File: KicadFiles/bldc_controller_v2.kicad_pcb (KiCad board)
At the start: 2 copper layers, 50 x 99 mm, 184 parts, among them J1 Conn_01x06_Male, J10 Conn_01x02_Female, J11 Conn_01x02_Female, J12 Conn_01x02_Female, J13 Conn_01x02_Female, J14 Conn_01x02_Female, J15 Conn_01x04_Male, J2 Conn_01x03_Male, J3 Conn_01x03_Male, J4 Screw_Terminal, J5 Conn_01x02_Female, J9 Conn_01x02_Female, Q1 DMN65D8L-7, Q10 IRLB8721PBF, Q11 IRLB8721PBF, Q2 DMN65D8L-7, Q3 DMN65D8L-7, Q4 DMN65D8L-7, Q5 IRF4905, Q6 IRLB8721PBF, Q7 IRLB8721PBF, Q8 IRLB8721PBF, Q9 IRLB8721PBF, SW2 D6C40 F1 LFS, SW3 1301.9314, SW4 1301.9314, SW5 SW_Push_DPDT, U1 ATmega328P-PU, U2 uA7810, U3 LM7805_TO220, U4 MCP601-xP, U5 LM339, U6 IRS2004, U7 IRS2004, U8 IRS2004, U9 HCPL-181-00DE, Y1 9B-16.000MBBK-B

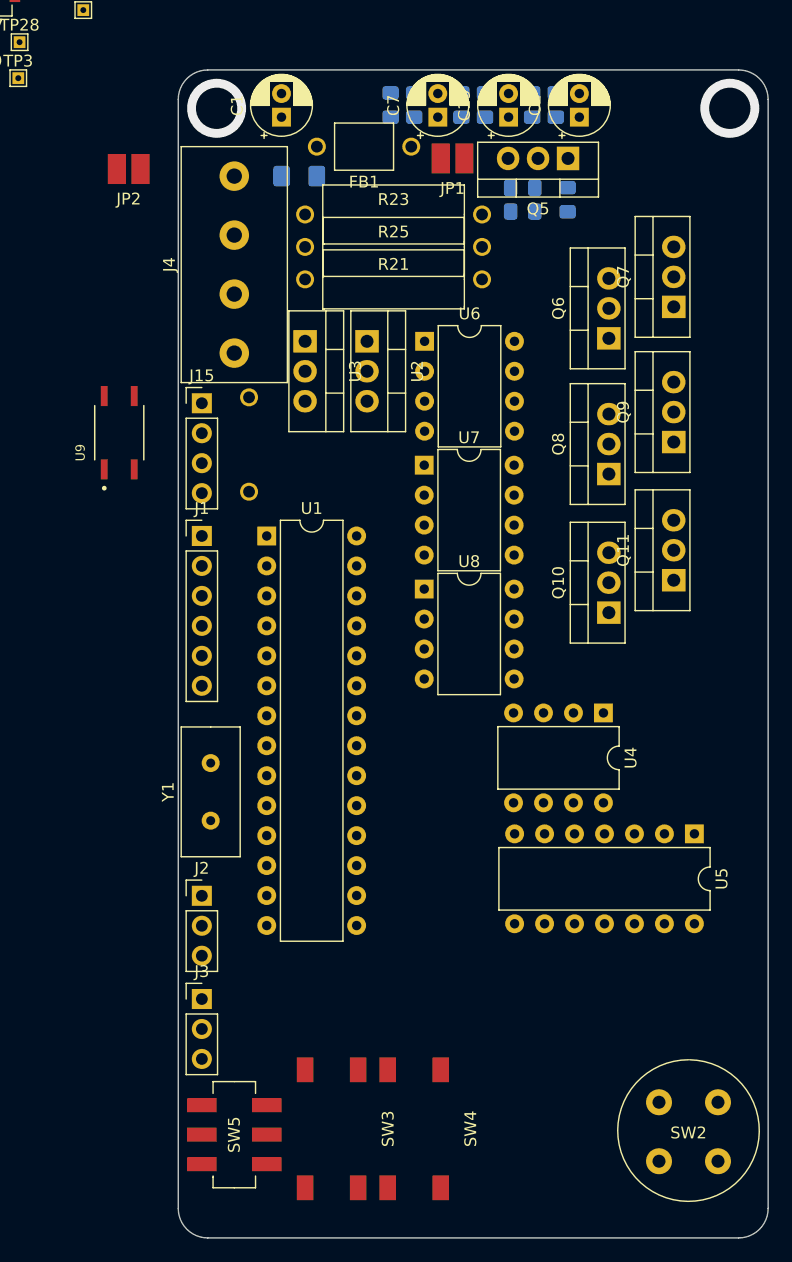
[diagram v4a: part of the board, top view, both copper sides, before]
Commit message: Updated Major Parts Placement
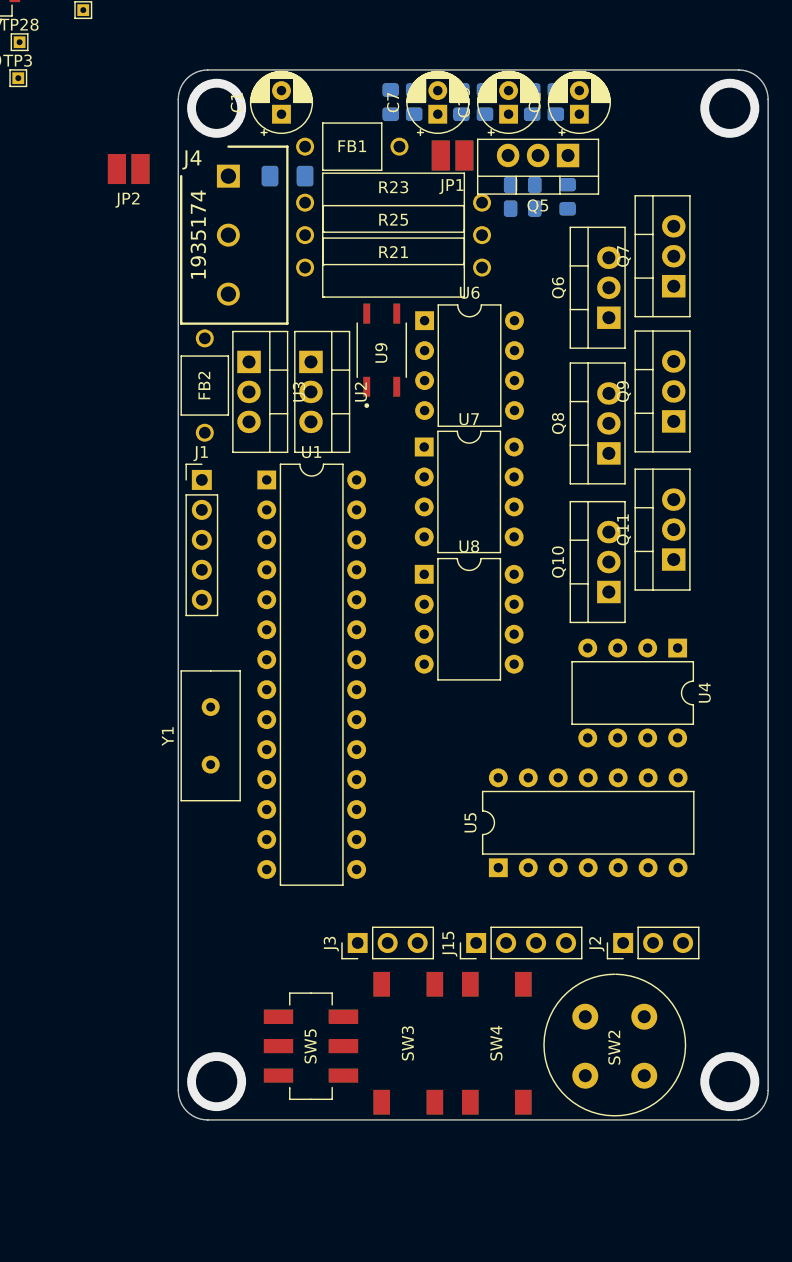
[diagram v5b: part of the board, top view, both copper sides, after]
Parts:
- FB2: moved to F.Cu
- J1: value Conn_01x06_Male -> Conn_01x05_Male; footprint Connector_PinHeader_2.54mm:PinHeader_1x06_P2.54mm_Vertical -> Connector_PinHeader_2.54mm:PinHeader_1x05_P2.54mm_Vertical
- J4: value Screw_Terminal -> 1935174; footprint Connector:Terminal_Block_4Pin_TH -> 1935174:SHDR3W110P0X500_1X3_1500X900X1140P
- moved J15 51.3 mm to (138.2, 135.0), turned to 90 degrees
- moved J2 35.9 mm to (150.7, 135.0), turned to 90 degrees
- moved U9 23.3 mm to (130.2, 84.8)
- moved U5 16.9 mm to (140.1, 128.6), turned to 90 degrees
- moved J3 14.0 mm to (128.2, 135.0), turned to 90 degrees
- moved SW4 10.1 mm to (142.2, 143.5)
- moved SW5 9.92 mm to (124.2, 143.8)
- moved SW3 9.74 mm to (134.8, 143.5)
- moved SW2 9.57 mm to (150.0, 146.2)
- moved U4 8.36 mm to (155.3, 110.0)
- moved J4 7.52 mm to (117.2, 70.0)
- moved FB2 6.25 mm to (115.2, 87.8)
- moved U2 5.06 mm to (124.2, 85.8)
- moved U3 5.06 mm to (119.0, 85.8)
- moved J1 4.75 mm to (115.0, 95.8)
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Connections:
- J1 pad 4: GNDD -> /TXD
- J1 pad 5: /TXD -> /RXD
- U5 pad 10: /NEUTRAL -> /I_SENSE
- U5 pad 11: /C_FILT -> /I_THRESH
- U5 pad 13: /BEMF_C -> Net-(R52-Pad1)
- U5 pad 2: Net-(R52-Pad1) -> /BEMF_C
- U5 pad 4: /I_SENSE -> /NEUTRAL
- U5 pad 5: /I_THRESH -> /C_FILT
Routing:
- net (no net): vias 2 -> 4
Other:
- board size 50 x 99 mm -> 50 x 89 mm

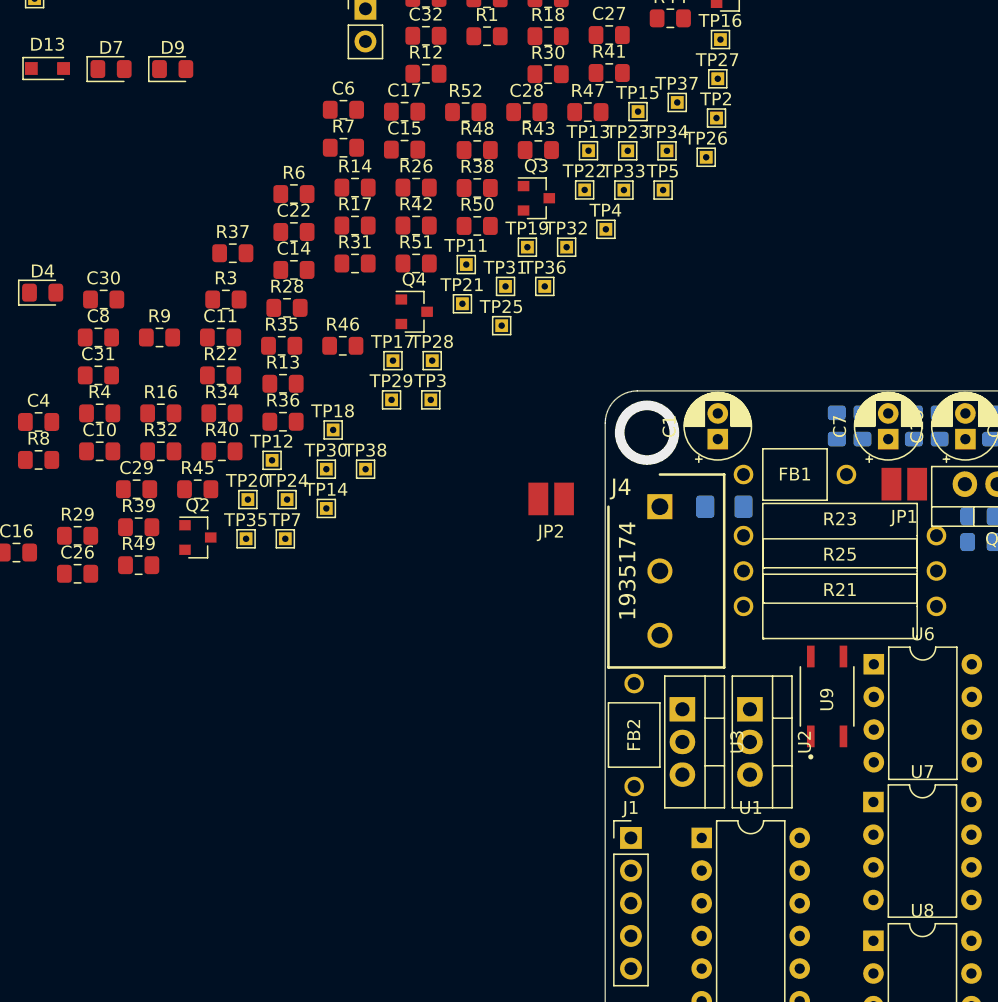
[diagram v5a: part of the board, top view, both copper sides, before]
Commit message: Replaced FB with Jumper
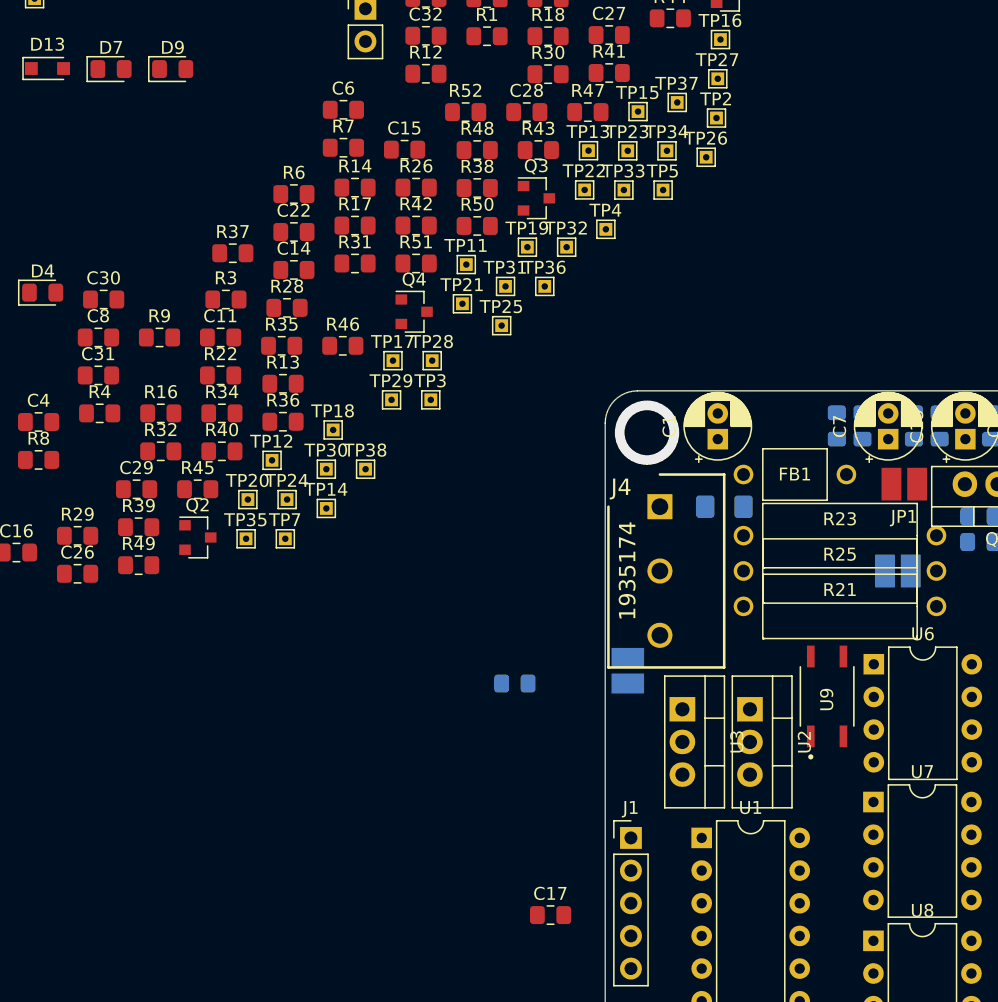
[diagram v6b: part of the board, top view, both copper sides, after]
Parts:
- removed FB2: BL01RN1A1D2B, Ferrite_THT:Ferrite_Bead_TH
- added JP3: SolderJumper_2_Open, Jumper:Solder_Jumper_2_Pin_5A, B.Cu at (114.8, 82.8)
- C10, JP2: moved to B.Cu
- moved C17 63.5 mm to (108.8, 101.8)
- moved C10 37.0 mm to (106.0, 83.8)
- moved JP2 27.5 mm to (135.8, 75.0)
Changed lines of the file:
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@@
     (add_net VBUS)
   )
+  (module Jumper:Solder_Jumper_2_Pin_5A (layer B.Cu)
+    (at 114.75 82.75 90)
+    (fp_text reference JP3 (at 0 -2.54 270) (layer B.SilkS)
+      (effects (font (size 1 1) (thickness 0.15)) (justify mirror))
+    )
+    (fp_text value SolderJumper_2_Open (at 0 -1.27 270) (layer B.Fab)
+      (effects (font (size 1 1) (thickness 0.15)) (justify mirror))
+    )
+    (pad 1 smd rect (at -1 0 90) (size 1.54 2.54) (layers B.Cu B.Paste B.Mask)
+      (net 4 GNDD))
+    (pad 2 smd rect (at 1 0 90) (size 1.54 2.54) (layers B.Cu B.Paste B.Mask)
+      (net 1 GNDPWR))
+  )
   (module Connector_PinHeader_2.54mm:PinHeader_1x05_P2.54mm_Vertical (layer F.Cu)
     (at 115 95.75)
@@
   )
   (module Ferrite_THT:Ferrite_Bead_TH (layer F.Cu)
-    (at 115.25 87.75 270)
-    (fp_text reference FB2 (at 0 0 90) (layer F.SilkS)
-      (effects (font (size 1 1) (thickness 0.15)))
-    )
-    (fp_text value BL01RN1A1D2B (at 0 3.1 90) (layer F.Fab)
-      (effects (font (size 1 1) (thickness 0.15)))
-    )
-    (fp_line (start 2.5 -2) (end -2.5 -2) (layer F.SilkS) (width 0.12))
-    (fp_line (start 2.5 2) (end 2.5 -2) (layer F.SilkS) (width 0.12))
-    (fp_line (start -2.5 2) (end 2.5 2) (layer F.SilkS) (width 0.12))
-    (fp_line (start -2.5 -2) (end -2.5 2) (layer F.SilkS) (width 0.12))
-    (pad 1 thru_hole circle (at -4 0 270) (size 1.524 1.524) (drill 1) (layers *.Cu *.Mask)
-      (net 1 GNDPWR))
-    (pad 2 thru_hole circle (at 4 0 270) (size 1.524 1.524) (drill 1) (layers *.Cu *.Mask)
-      (net 4 GNDD))
-  )
-  (module Ferrite_THT:Ferrite_Bead_TH (layer F.Cu)
     (at 127.75 67.5 180)
     (fp_text reference FB1 (at 0 0) (layer F.SilkS)
@@
     )
   )
-  (module Jumper:Solder_Jumper_2_Pin_5A (layer F.Cu)
-    (at 108.8 69.4)
-    (fp_text reference JP2 (at 0 2.54) (layer F.SilkS)
-      (effects (font (size 1 1) (thickness 0.15)))
+  (module Jumper:Solder_Jumper_2_Pin_5A (layer B.Cu)
+    (at 135.75 75)
+    (fp_text reference JP2 (at 0 -2.54) (layer B.SilkS)
+      (effects (font (size 1 1) (thickness 0.15)) (justify mirror))
     )
-    (fp_text value SolderJumper_2_Open (at 0 1.27) (layer F.Fab)
-      (effects (font (size 1 1) (thickness 0.15)))
+    (fp_text value SolderJumper_2_Open (at 0 -1.27) (layer B.Fab)
+      (effects (font (size 1 1) (thickness 0.15)) (justify mirror))
     )
-    (pad 1 smd rect (at -1 0) (size 1.54 2.54) (layers F.Cu F.Paste F.Mask)
+    (pad 1 smd rect (at -1 0) (size 1.54 2.54) (layers B.Cu B.Paste B.Mask)
       (net 1 GNDPWR))
-    (pad 2 smd rect (at 1 0) (size 1.54 2.54) (layers F.Cu F.Paste F.Mask)
+    (pad 2 smd rect (at 1 0) (size 1.54 2.54) (layers B.Cu B.Paste B.Mask)
       (net 47 /I_RAW))
   )
@@
   )
   (module Capacitor_SMD:C_0805_2012Metric_Pad1.15x1.40mm_HandSolder (layer F.Cu)
-    (at 97.400225 39.296)
+    (at 108.75 101.75)
     (descr "Capacitor SMD 0805 (2012 Metric), square (rectangular) end terminal, IPC_7351 nominal with elongated pad for handsoldering. (Body size source: https://docs.google.com/spreadsheets/d/1BsfQQcO9C6DZCsRaXUlFlo91Tg2WpOkGARC1WS5S8t0/edit?usp=sharing), generated with kicad-footprint-generator")
     (tags "capacitor handsolder")
@@
     )
   )
-  (module Capacitor_SMD:C_0805_2012Metric_Pad1.15x1.40mm_HandSolder (layer F.Cu)
-    (at 73.700225 65.696)
+  (module Capacitor_SMD:C_0805_2012Metric_Pad1.15x1.40mm_HandSolder (layer B.Cu)
+    (at 105.975 83.75)
     (descr "Capacitor SMD 0805 (2012 Metric), square (rectangular) end terminal, IPC_7351 nominal with elongated pad for handsoldering. (Body size source: https://docs.google.com/spreadsheets/d/1BsfQQcO9C6DZCsRaXUlFlo91Tg2WpOkGARC1WS5S8t0/edit?usp=sharing), generated with kicad-footprint-generator")
     (tags "capacitor handsolder")
     (attr smd)
-    (fp_text reference C10 (at 0 -1.65) (layer F.SilkS)
-      (effects (font (size 1 1) (thickness 0.15)))
+    (fp_text reference C10 (at 0 1.65) (layer B.SilkS)
+      (effects (font (size 1 1) (thickness 0.15)) (justify mirror))
     )
-    (fp_text value 1uF (at 0 1.65) (layer F.Fab)
-      (effects (font (size 1 1) (thickness 0.15)))
+    (fp_text value 1uF (at 0 -1.65) (layer B.Fab)
+      (effects (font (size 1 1) (thickness 0.15)) (justify mirror))
     )
-    (fp_text user %R (at 0 0) (layer F.Fab)
-      (effects (font (size 0.5 0.5) (thickness 0.08)))
+    (fp_line (start -1 -0.6) (end -1 0.6) (layer B.Fab) (width 0.1))
+    (fp_line (start -1 0.6) (end 1 0.6) (layer B.Fab) (width 0.1))
+    (fp_line (start 1 0.6) (end 1 -0.6) (layer B.Fab) (width 0.1))
+    (fp_line (start 1 -0.6) (end -1 -0.6) (layer B.Fab) (width 0.1))
+    (fp_line (start -0.261252 0.71) (end 0.261252 0.71) (layer B.SilkS) (width 0.12))
+    (fp_line (start -0.261252 -0.71) (end 0.261252 -0.71) (layer B.SilkS) (width 0.12))
+    (fp_line (start -1.85 -0.95) (end -1.85 0.95) (layer B.CrtYd) (width 0.05))
+    (fp_line (start -1.85 0.95) (end 1.85 0.95) (layer B.CrtYd) (width 0.05))
+    (fp_line (start 1.85 0.95) (end 1.85 -0.95) (layer B.CrtYd) (width 0.05))
+    (fp_line (start 1.85 -0.95) (end -1.85 -0.95) (layer B.CrtYd) (width 0.05))
+    (fp_text user %R (at 0 0) (layer B.Fab)
+      (effects (font (size 0.5 0.5) (thickness 0.08)) (justify mirror))
     )
-    (fp_line (start 1.85 0.95) (end -1.85 0.95) (layer F.CrtYd) (width 0.05))
-    (fp_line (start 1.85 -0.95) (end 1.85 0.95) (layer F.CrtYd) (width 0.05))
-    (fp_line (start -1.85 -0.95) (end 1.85 -0.95) (layer F.CrtYd) (width 0.05))
-    (fp_line (start -1.85 0.95) (end -1.85 -0.95) (layer F.CrtYd) (width 0.05))
-    (fp_line (start -0.261252 0.71) (end 0.261252 0.71) (layer F.SilkS) (width 0.12))
-    (fp_line (start -0.261252 -0.71) (end 0.261252 -0.71) (layer F.SilkS) (width 0.12))
-    (fp_line (start 1 0.6) (end -1 0.6) (layer F.Fab) (width 0.1))
-    (fp_line (start 1 -0.6) (end 1 0.6) (layer F.Fab) (width 0.1))
-    (fp_line (start -1 -0.6) (end 1 -0.6) (layer F.Fab) (width 0.1))
-    (fp_line (start -1 0.6) (end -1 -0.6) (layer F.Fab) (width 0.1))
-    (pad 2 smd roundrect (at 1.025 0) (size 1.15 1.4) (layers F.Cu F.Paste F.Mask) (roundrect_rratio 0.217391)
-      (net 4 GNDD))
-    (pad 1 smd roundrect (at -1.025 0) (size 1.15 1.4) (layers F.Cu F.Paste F.Mask) (roundrect_rratio 0.217391)
+    (pad 1 smd roundrect (at -1.025 0) (size 1.15 1.4) (layers B.Cu B.Paste B.Mask) (roundrect_rratio 0.217391)
       (net 7 +12V))
+    (pad 2 smd roundrect (at 1.025 0) (size 1.15 1.4) (layers B.Cu B.Paste B.Mask) (roundrect_rratio 0.217391)
+      (net 4 GNDD))
     (model ${KISYS3DMOD}/Capacitor_SMD.3dshapes/C_0805_2012Metric.wrl
       (at (xyz 0 0 0))

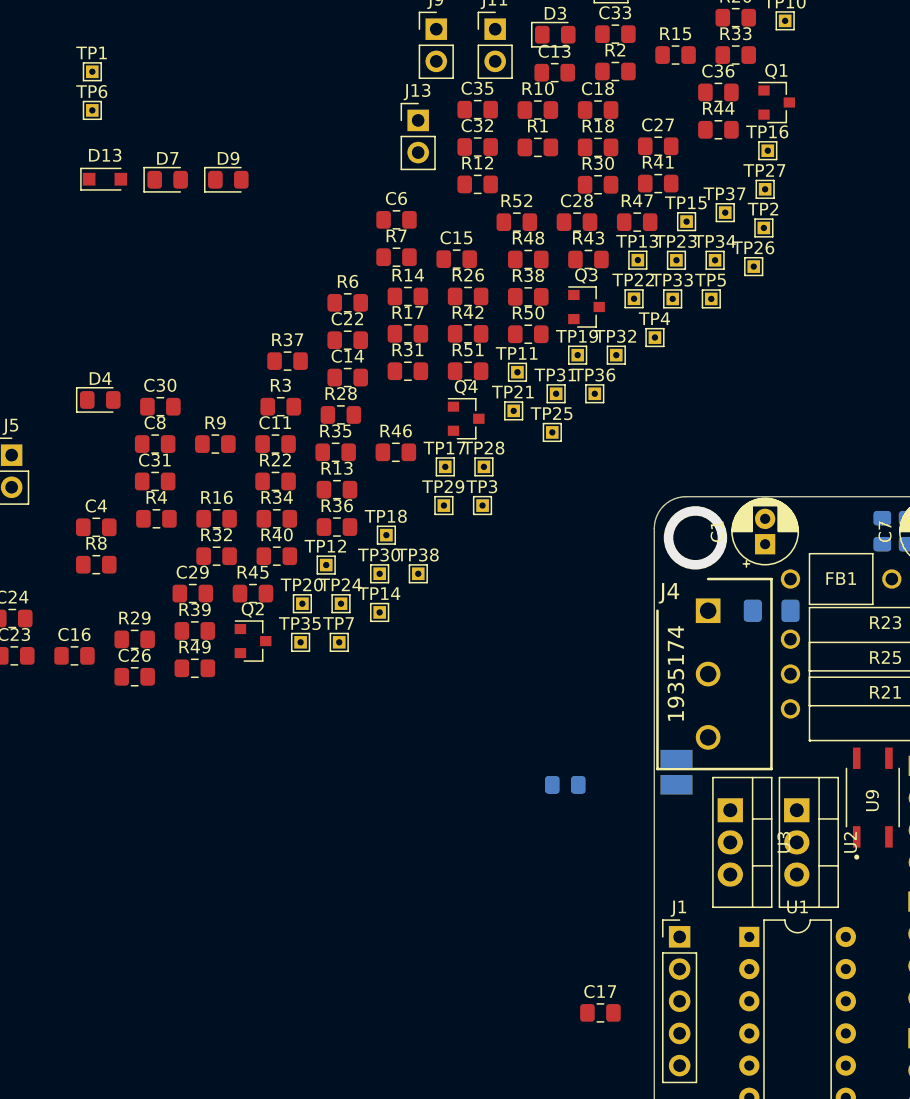
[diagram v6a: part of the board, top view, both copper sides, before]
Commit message: Updated 5V Regulator
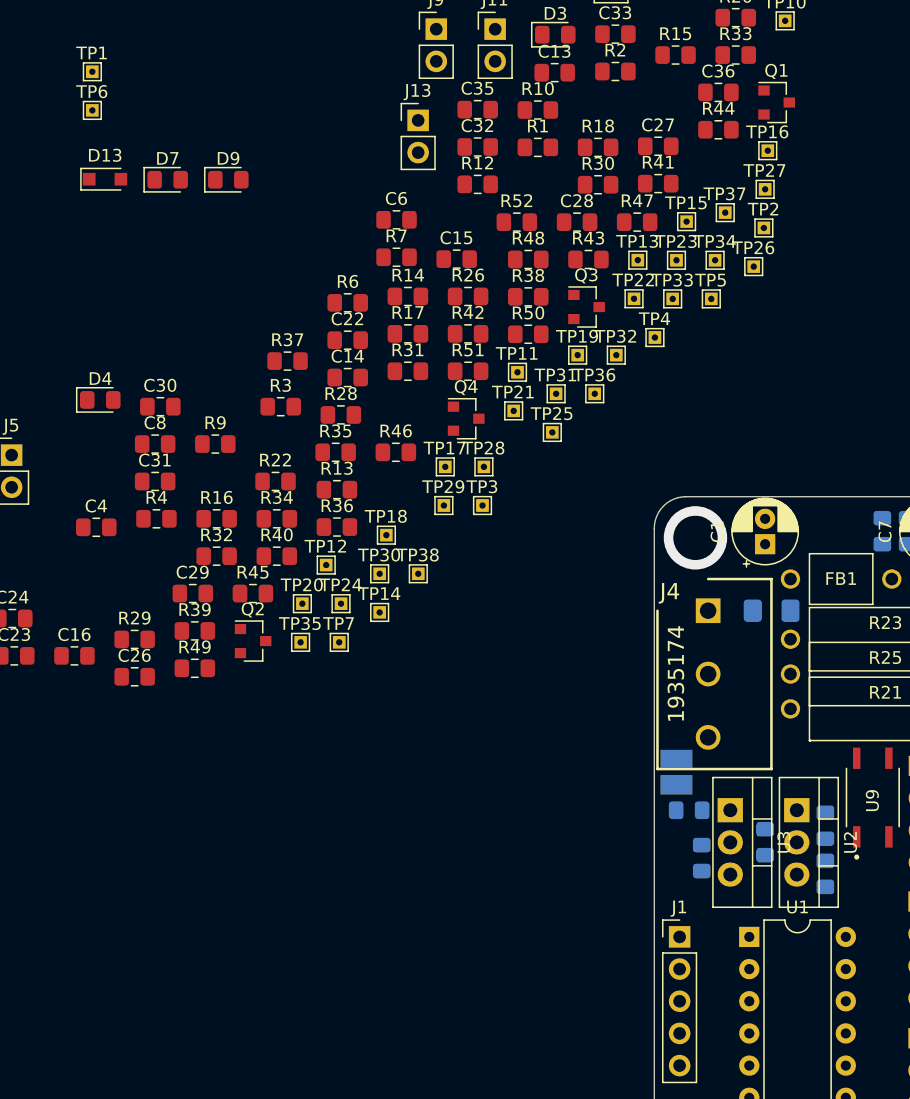
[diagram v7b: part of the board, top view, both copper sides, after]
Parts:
- C11, C17, C18, R8: moved to B.Cu
- moved C18 59.6 mm to (116.8, 89.5), turned to 90 degrees
- moved R8 57.2 mm to (121.8, 88.3), turned to 270 degrees
- moved C11 43.6 mm to (115.8, 85.8), turned to 180 degrees
- moved C17 20.9 mm to (126.5, 90.8), turned to 90 degrees
- moved C10 20.8 mm to (126.5, 87.0), turned to 270 degrees
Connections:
- C11 pad 1: +10V -> Net-(C11-Pad1)
- R8 pad 1: Net-(R8-Pad1) -> Net-(C11-Pad1)
- U3 pad 1: Net-(R8-Pad1) -> Net-(C11-Pad1)
